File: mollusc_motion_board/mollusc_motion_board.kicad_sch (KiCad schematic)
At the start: 27 parts, among them J2 Barrel_Jack_Switch 12V, J3 RJ45 x4, SW1 SW_Push, SW2 SW_Push, U5 Teensy4.0, U6 74HC14, U7 74HC14, U8 LM7805_TO220

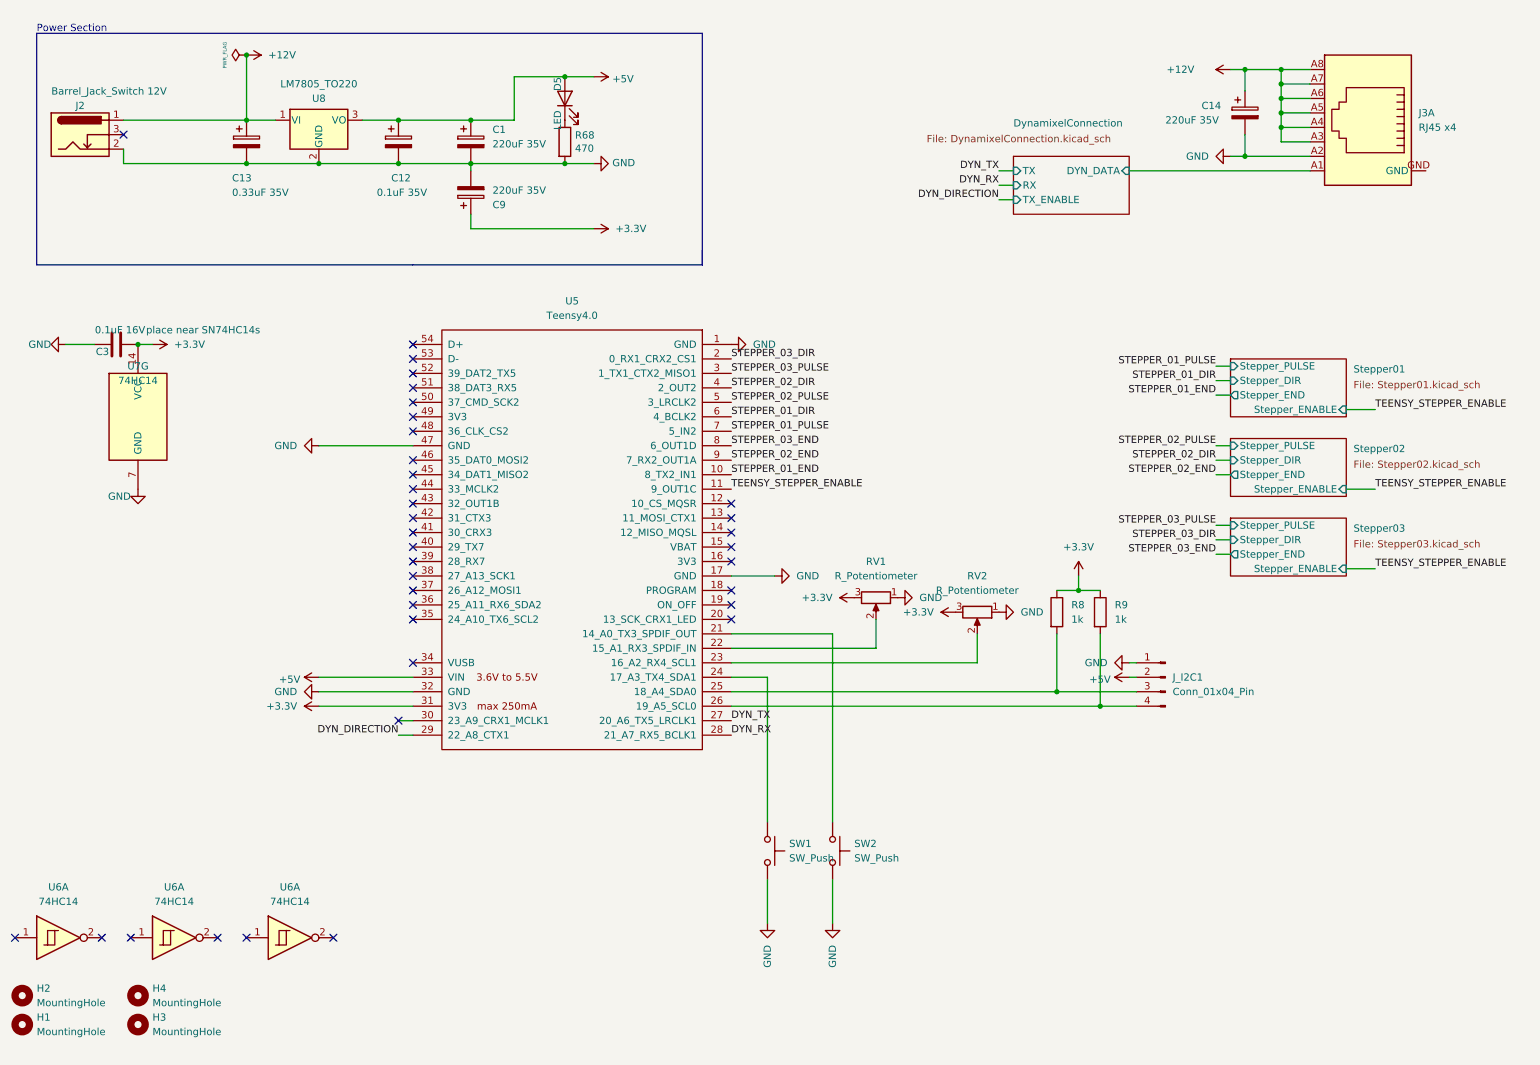
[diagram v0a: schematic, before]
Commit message: adding BOM
renaming to 'mollusc_motion'
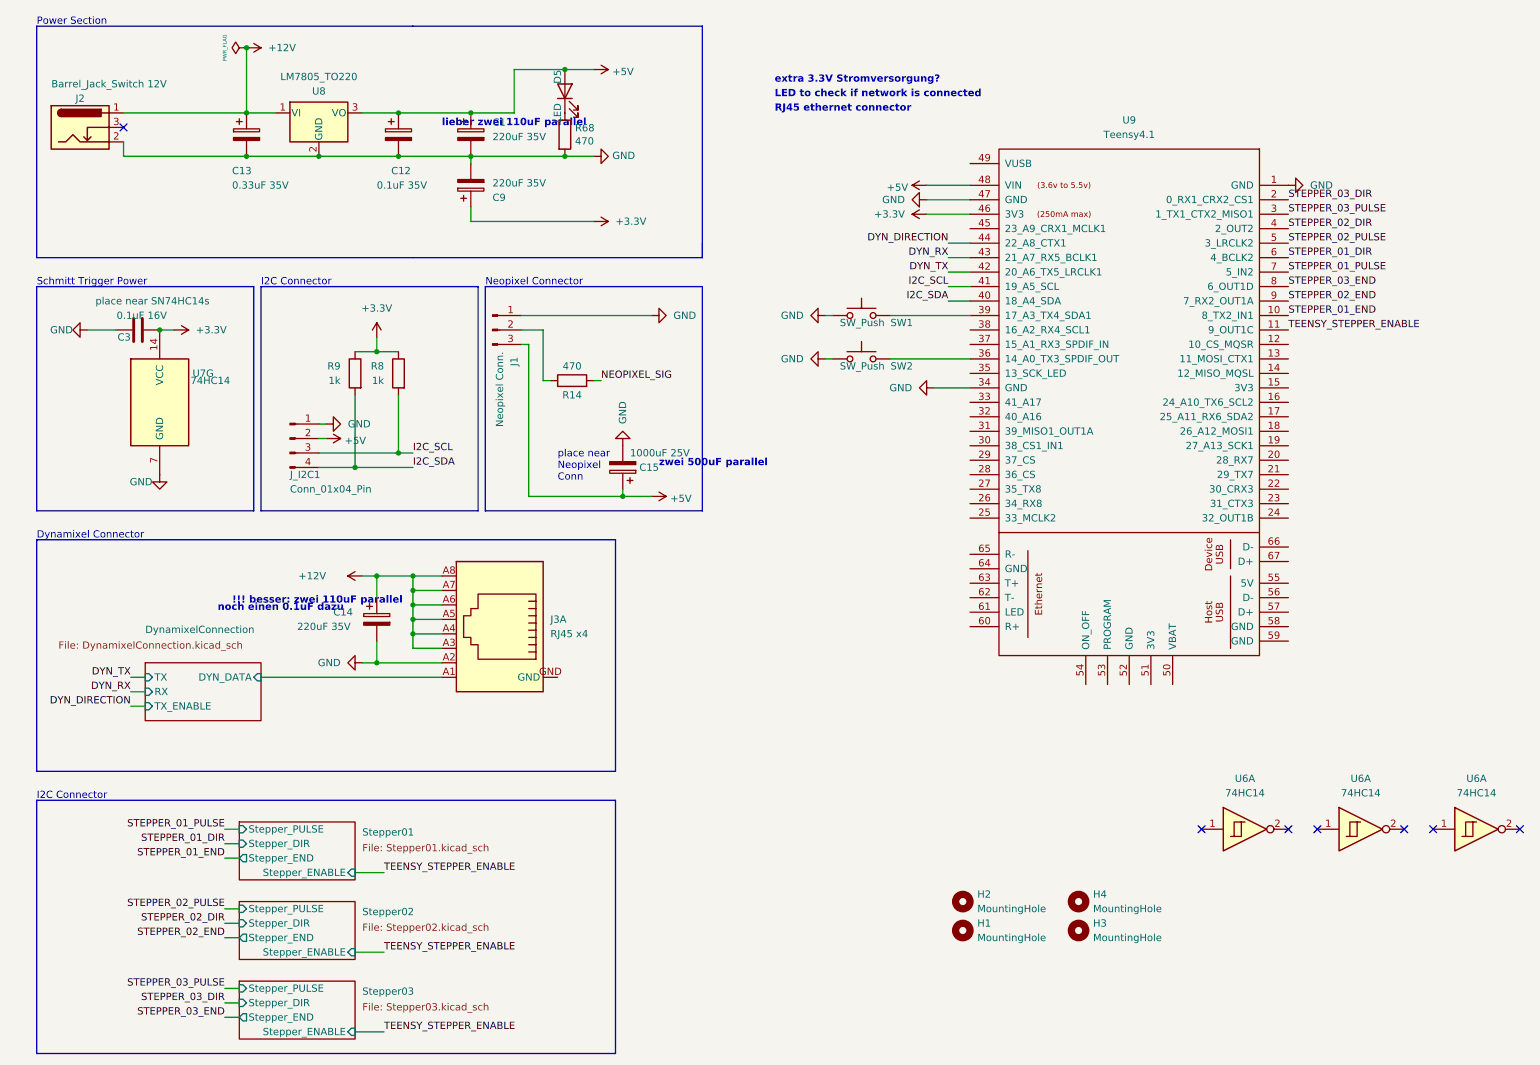
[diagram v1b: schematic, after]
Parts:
- removed RV1, RV2: R_Potentiometer, Potentiometer_THT:Potentiometer_TT_P0915N, symbol Device:R_Potentiometer
- removed U5: Teensy4.0, teensy:Teensy40, symbol teensy:Teensy4.0
- added C15: 1000uF 25V, Capacitor_THT:CP_Radial_D10.0mm_P5.00mm, symbol Device:C_Polarized
- added J1: Neopixel Conn., Connector_PinHeader_2.54mm:PinHeader_1x03_P2.54mm_Vertical, symbol Connector:Conn_01x03_Pin
- added R14: 470, HangOn_Mainboard:R0603, symbol Device:R
- added U9: Teensy4.1, teensy:Teensy41, symbol teensy:Teensy4.1
- C12: footprint HangOn_Mainboard:C0805 -> HangOn_Mainboard:R0603; JLCPCB Part # C49678 -> (none)
- C13: footprint HangOn_Mainboard:C0805 -> HangOn_Mainboard:R0603; JLCPCB Part # C1740 -> (none)
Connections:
- net +3.3V: now also U9.46 (3V3)
- net +5V: now also C15.1, J1.3 (Pin_3), U9.48 (VIN)
- net DYN_DIRECTION: now also U9.44 (22_A8_CTX1)
- net DYN_RX: now also U9.43 (21_A7_RX5_BCLK1)
- net DYN_TX: now also U9.42 (20_A6_TX5_LRCLK1)
- net GND: now also SW1.1, SW2.1, C15.2, J1.1 (Pin_1), U9.1 (GND), U9.34 (GND), U9.47 (GND); no longer SW1.2, SW2.2
- net STEPPER_01_DIR: now also U9.6 (4_BCLK2)
- net STEPPER_01_END: now also U9.10 (8_TX2_IN1)
- net STEPPER_01_PULSE: now also U9.7 (5_IN2)
- net STEPPER_02_DIR: now also U9.4 (2_OUT2)
- net STEPPER_02_END: now also U9.9 (7_RX2_OUT1A)
- net STEPPER_02_PULSE: now also U9.5 (3_LRCLK2)
- net STEPPER_03_DIR: now also U9.2 (0_RX1_CRX2_CS1)
- net STEPPER_03_END: now also U9.8 (6_OUT1D)
- net STEPPER_03_PULSE: now also U9.3 (1_TX1_CTX2_MISO1)
- net TEENSY_STEPPER_ENABLE: now also U9.11 (9_OUT1C)
- net I2C_SCL: now reaches J_I2C1.3 (Pin_3), R8.2
- net I2C_SCL: now also U9.41 (19_A5_SCL)
- net I2C_SDA: now reaches J_I2C1.4 (Pin_4), R9.2
- net I2C_SDA: now also U9.40 (18_A4_SDA)
- new net: SW2.2, U9.36 (14_A0_TX3_SPDIF_OUT)
- new net: SW1.2, U9.39 (17_A3_TX4_SDA1)
- new net: J1.2 (Pin_2), R14.1
- new net NEOPIXEL_SIG: R14.2
- no-connect marks 36 -> 7
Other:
- note added: "!!! besser: zwei 110uF parallel"
- note added: "Dynamixel Connector"
- note added: "I2C Connector"
- note added: "LED to check if network is connected"
- note added: "Neopixel Connector"
- note added: "RJ45 ethernet connector"
- note added: "Schmitt Trigger Power"
- note added: "extra 3.3V Stromversorgung?"
- note added: "lieber zwei 110uF parallel"
- note added: "noch einen 0.1uF dazu"
- note added: "place near Neopixel Conn"
- note added: "zwei 500uF parallel"
- moved on the sheet: C1, C12, C13, C14, C3, C9, D5, H1, H2, H3, H4, J2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

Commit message: adding ethernet jack
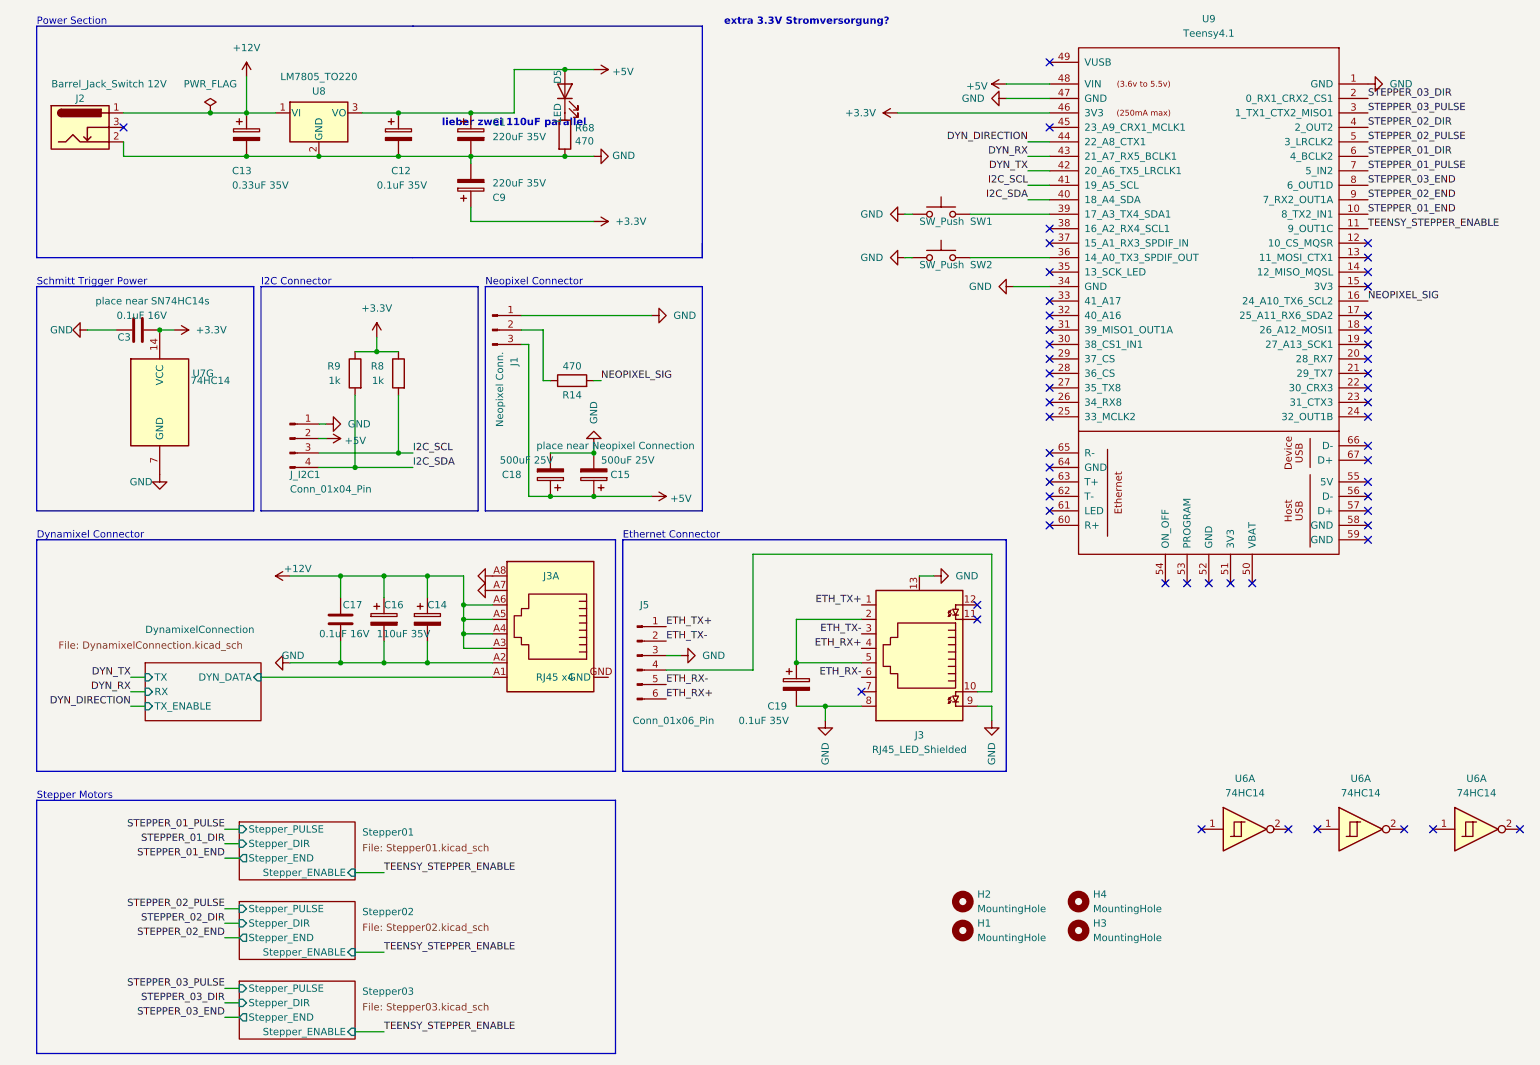
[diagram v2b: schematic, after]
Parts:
- added C16: 110uF 35V, symbol Device:C_Polarized
- added C17: 0.1uF 16V, HangOn_Mainboard:R0603, symbol Device:C
- added C18: 500uF 25V, Capacitor_THT:CP_Radial_D10.0mm_P5.00mm, symbol Device:C_Polarized
- added C19: 0.1uF 35V, HangOn_Mainboard:R0603, symbol Device:C_Polarized
- added J3: RJ45_LED_Shielded, Connector_RJ:RJ45_Cetus_J1B1211CCD_Horizontal, symbol Connector:RJ45_LED_Shielded
- added J5: Conn_01x06_Pin, Connector_PinHeader_2.00mm:PinHeader_2x03_P2.00mm_Vertical, symbol Connector:Conn_01x06_Pin
- C14: value 220uF 35V -> 110uF 35V; footprint HangOn_Mainboard:CAP-SMD_BD8.0-L8.3-W8.3-LS9.9-FD -> (none); JLCPCB Part # C178594 -> (none)
- C15: value 1000uF 25V -> 500uF 25V; Comment (none) -> place near Neopixel Connection
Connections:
- net +12V: now also C16.1, C17.2; no longer J3.A7, J3.A8
- net +5V: now also C18.1
- net GND: now also J3.A7, J3.A8, C16.2, C17.1, C18.2, C19.2, J3.13, J3.8, J3.9, J5.3 (Pin_3)
- net NEOPIXEL_SIG: now also U9.16 (24_A10_TX6_SCL2)
- new net: J3.10, J5.4 (Pin_4)
- new net: C19.1, J3.2, J3.5
- new net ETH_RX+: J3.4, J5.6 (Pin_6)
- new net ETH_RX-: J3.6, J5.5 (Pin_5)
- new net ETH_TX+: J3.1, J5.1 (Pin_1)
- new net ETH_TX-: J3.3, J5.2 (Pin_2)
- no-connect marks 7 -> 54
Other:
- note added: "Ethernet Connector"
- note added: "Stepper Motors"
- note removed: "!!! besser: zwei 110uF parallel"
- note removed: "LED to check if network is connected"
- note removed: "RJ45 ethernet connector"
- note removed: "noch einen 0.1uF dazu"
- note removed: "place near Neopixel Conn"
- note removed: "zwei 500uF parallel"
- moved on the sheet: C14, C15, J3A, SW1, SW2, U9

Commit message: Board v2 wip
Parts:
- removed U8: LM7805_TO220, HangOn_Mainboard:TO-252-2_L6.5-W6.1-P4.58-LS10.0-TL, symbol Regulator_Linear:LM7805_TO220
- added BT1: Battery_Cell, molluscmotion:BAT_S8421-45R, symbol Device:Battery_Cell
- added D3: SMAJ14A_C908768, molluscmotion:SMA_L4.3-W2.6-LS5.1-RD, symbol molluscmotion:SMAJ14A_C908768
- added D5: LED, molluscmotion:LED0603-RD, symbol Device:LED
- added J6: D36V50F5, clockdiv:Pololu_5V_5.5A_Step-Down_Voltage_Regulator_D36V50F5, symbol clockdiv:Pololu_5V,_5.5A_Step-Down_Voltage_Regulator_D36V50F5
- added J7: Endswitches Test Conn, Connector_PinHeader_2.54mm:PinHeader_1x03_P2.54mm_Vertical, symbol Connector:Conn_01x03_Pin
- added R68: 510, molluscmotion:R0603, symbol Device:R
- added TP1: TP12V, TestPoint:TestPoint_THTPad_2.5x2.5mm_Drill1.2mm, symbol Connector:TestPoint
- added TP2: TPGND, TestPoint:TestPoint_THTPad_2.5x2.5mm_Drill1.2mm, symbol Connector:TestPoint
- added TP3: TP5V, TestPoint:TestPoint_THTPad_2.5x2.5mm_Drill1.2mm, symbol Connector:TestPoint
- added TP4: TP3V3, TestPoint:TestPoint_THTPad_2.5x2.5mm_Drill1.2mm, symbol Connector:TestPoint
- C1, C9: footprint HangOn_Mainboard:CAP-SMD_BD8.0-L8.3-W8.3-LS9.9-FD -> molluscmotion:CAP-SMD_BD8.0-L8.3-W8.3-LS9.9-FD
- C12: value 0.1uF 35V -> 220uF 35V; footprint HangOn_Mainboard:R0603 -> molluscmotion:CAP-SMD_BD8.0-L8.3-W8.3-LS9.9-FD; JLCPCB Part # (none) -> C178594
- C13: value 0.33uF 35V -> 220uF 35V; footprint HangOn_Mainboard:R0603 -> molluscmotion:CAP-SMD_BD8.0-L8.3-W8.3-LS9.9-FD; JLCPCB Part # (none) -> C178594
- C14, C16: footprint (none) -> molluscmotion:CAP-SMD_BD6.3-L6.6-W6.6-LS7.2-FD; JLCPCB Part # (none) -> C401811
- C15, C18: value 500uF 25V -> 1000uF 25V
- C17, C3: value 0.1uF 16V -> 0.1uF 50V; footprint HangOn_Mainboard:R0603 -> molluscmotion:C0603
- C19: value 0.1uF 35V -> 0.1uF 50V; footprint HangOn_Mainboard:R0603 -> molluscmotion:C0603; JLCPCB Part # (none) -> C14663
- D5: footprint HangOn_Mainboard:LED1206-R-RD_WHITE -> molluscmotion:LED0603-RD; JLCPCB Part # C434441 -> C2286
- H1, H2, H3, H4: footprint MountingHole:MountingHole_3.2mm_M3_DIN965_Pad -> MountingHole:MountingHole_3.2mm_M3_DIN965_Pad_TopBottom
- R14: footprint HangOn_Mainboard:R0603 -> molluscmotion:R0603; JLCPCB Part # (none) -> C23179
- R68: value 470 -> 220; footprint HangOn_Mainboard:R0603 -> molluscmotion:R0603; JLCPCB Part # C23179 -> C22962
- R8, R9: footprint HangOn_Mainboard:R0603 -> molluscmotion:R0603
- SW1, SW2: footprint HangOn_Mainboard:KEY-SMD_4P-L6.1-W6.1-P4.50-LS9.0 -> molluscmotion:KEY-SMD_4P-L6.1-W6.1-P4.50-LS9.0
- U6, U7: footprint HangOn_Mainboard:SOIC-14_L8.7-W3.9-P1.27-LS6.0-BL -> molluscmotion:SOIC-14_L8.7-W3.9-P1.27-LS6.0-BL
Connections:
- net +12V: now also J6.4 (Vrp); no longer C13.1, J2.1
- net +3.3V: now also TP4.1
- net +5V: now also C13.1, J6.1 (Vout), TP3.1; no longer C12.1
- net GND: now also J3.GND, D3.2, J6.2 (GND), R68.2, TP2.1
- net STEPPER_01_END: now also U9.8 (6_OUT1D), J7.1 (Pin_1); no longer U9.10 (8_TX2_IN1)
- net STEPPER_02_END: now also J7.2 (Pin_2)
- net STEPPER_03_END: now also U9.10 (8_TX2_IN1), J7.3 (Pin_3); no longer U9.8 (6_OUT1D)
- net at U9.50 (VBAT): now also BT1.1 (+)
- net at U9.52 (GND): now also BT1.2 (-)
- new net: D5.1 (K), R68.1
- new net Vin: C12.1, D3.1, D5.2 (A), J2.1, J6.3 (Vin), TP1.1
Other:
- note added: "160 Ohm"
- note added: "510 Ohm"
- note added: "powers dynamixel servos (max. 14.8V)"
- note removed: "lieber zwei 110uF parallel"
- moved on the sheet: C1, C15, C18, C9, D5, R68

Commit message: PCB v1.2 Layout
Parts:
- removed C16: 110uF 35V, molluscmotion:CAP-SMD_BD6.3-L6.6-W6.6-LS7.2-FD, symbol Device:C_Polarized
- added C16: 0.1uF 50V, molluscmotion:C0603, symbol Device:C
- added C20: 220uF 35V, molluscmotion:CAP-SMD_BD8.0-L8.3-W8.3-LS9.9-FD, symbol Device:C_Polarized
- C14: value 110uF 35V -> 220uF 35V; footprint molluscmotion:CAP-SMD_BD6.3-L6.6-W6.6-LS7.2-FD -> molluscmotion:CAP-SMD_BD8.0-L8.3-W8.3-LS9.9-FD; JLCPCB Part # C401811 -> C178594
- TP1, TP2, TP3, TP4: footprint TestPoint:TestPoint_THTPad_2.5x2.5mm_Drill1.2mm -> TestPoint:TestPoint_THTPad_1.5x1.5mm_Drill0.7mm
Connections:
- net +12V: now also C20.1
- net GND: now also C20.2
- net at U9.36 (14_A0_TX3_SPDIF_OUT): no longer SW2.2
- net at U9.38 (16_A2_RX4_SCL1): now also SW2.2
- net BAT+: now reaches BT1.1 (+), U9.50 (VBAT)
- net BAT+: now also C16.1
- net BAT-: now reaches BT1.2 (-), U9.52 (GND)
- net BAT-: now also C16.2
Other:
- moved on the sheet: BT1, D3

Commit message: PCB v1.2
v1.2, produced by JLCPCB
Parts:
- removed J7: Endswitches Test Conn, Connector_PinHeader_2.54mm:PinHeader_1x03_P2.54mm_Vertical, symbol Connector:Conn_01x03_Pin
- removed SW1, SW2: SW_Push, molluscmotion:KEY-SMD_4P-L6.1-W6.1-P4.50-LS9.0, symbol Switch:SW_Push
- added CB1, CB2: CircuitBreaker_1P_closed, clockdiv:CircuitBreaker_0603_closed, symbol clockdiv:CircuitBreaker_1P_closed
- added H5, H6: MountingHole, MountingHole:MountingHole_3.2mm_M3_DIN965_Pad, symbol Mechanical:MountingHole
- added J7, J8: NP Power, Connector_PinHeader_2.54mm:PinHeader_1x02_P2.54mm_Vertical, symbol Connector:Conn_01x02_Pin
- added TP_END_S1, TP_END_S2, TP_END_S3: TestPoint, TestPoint:TestPoint_THTPad_1.5x1.5mm_Drill0.7mm, symbol Connector:TestPoint
- added U5, U8: TSA063G60-250, molluscmotion:KEY-SMD_4P-L6.1-W6.1-P4.50-LS9.0, symbol molluscmotion:TSA063G60-250
- D3: value SMAJ14A_C908768 -> SMAJ14A
- H1, H2, H3, H4: footprint MountingHole:MountingHole_3.2mm_M3_DIN965_Pad_TopBottom -> MountingHole:MountingHole_3.2mm_M3_DIN965_Pad
- J1: value Neopixel Conn. -> NP Power+Sig
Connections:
- net +12V: no longer J3.A6
- net +5V: now also J1.1 (Pin_1), J7.1 (Pin_1), J8.1 (Pin_1); no longer J1.3 (Pin_3)
- net GND: now also J1.2 (Pin_2), J3.A6, CB1.1, CB2.1, J7.2 (Pin_2), J8.2 (Pin_2), U5.1, U8.1; no longer J1.1 (Pin_1), R68.2, R68.2
- net STEPPER_01_END: now also TP_END_S1.1
- net STEPPER_02_END: now also TP_END_S2.1
- net STEPPER_03_END: now also TP_END_S3.1
- net at U9.38 (16_A2_RX4_SCL1): now also U8.3
- net at U9.39 (17_A3_TX4_SDA1): now also U5.3
- net at R14.1: now also J1.3 (Pin_3); no longer J1.2 (Pin_2)
- new net: CB2.2, R68.2
- new net: CB1.2, R68.2
- no-connect marks 54 -> 58
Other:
- note added: "cut and replace with resistor to dim the led"
- note added: "power dynamixel servos 14.8V max"
- note removed: "powers dynamixel servos (max. 14.8V)"
- moved on the sheet: C1, C12, C13, C15, C18, D3, D5, J1, J2, R14, R68, TP1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
